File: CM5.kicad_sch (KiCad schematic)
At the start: 12 parts, among them J7 USB_B_Mini, J8 484060001, U6 Compute_Module_5_Functional

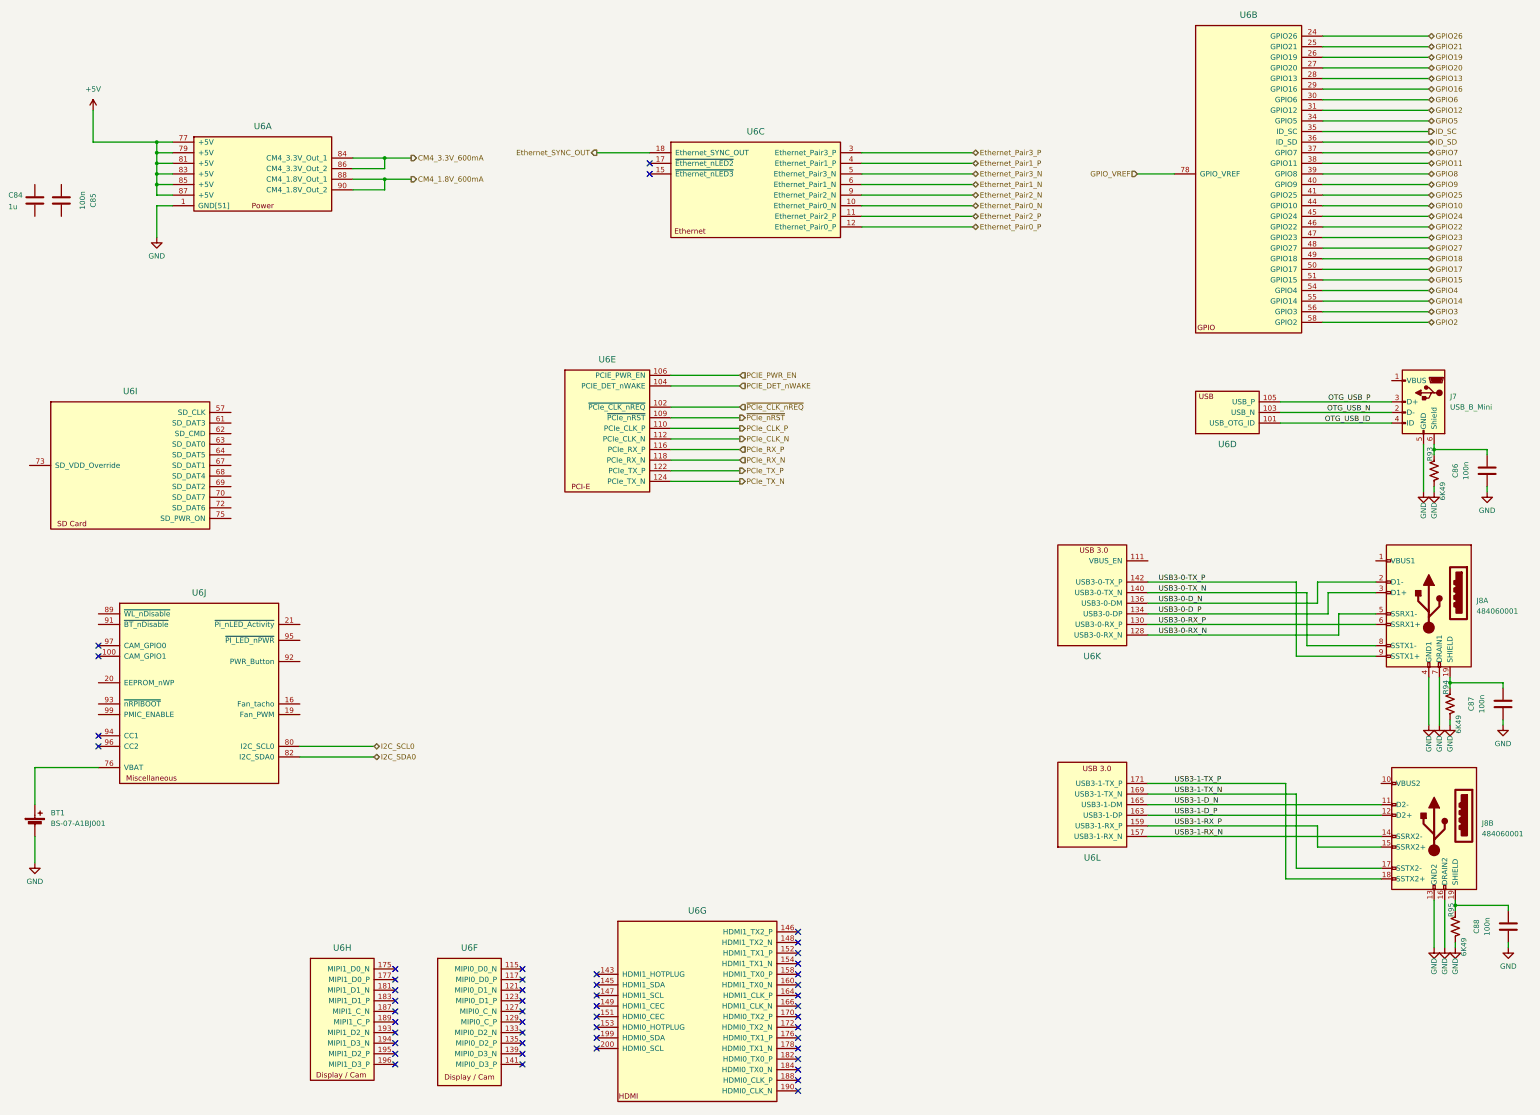
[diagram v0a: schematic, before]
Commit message: add impedance spec in the datasheet
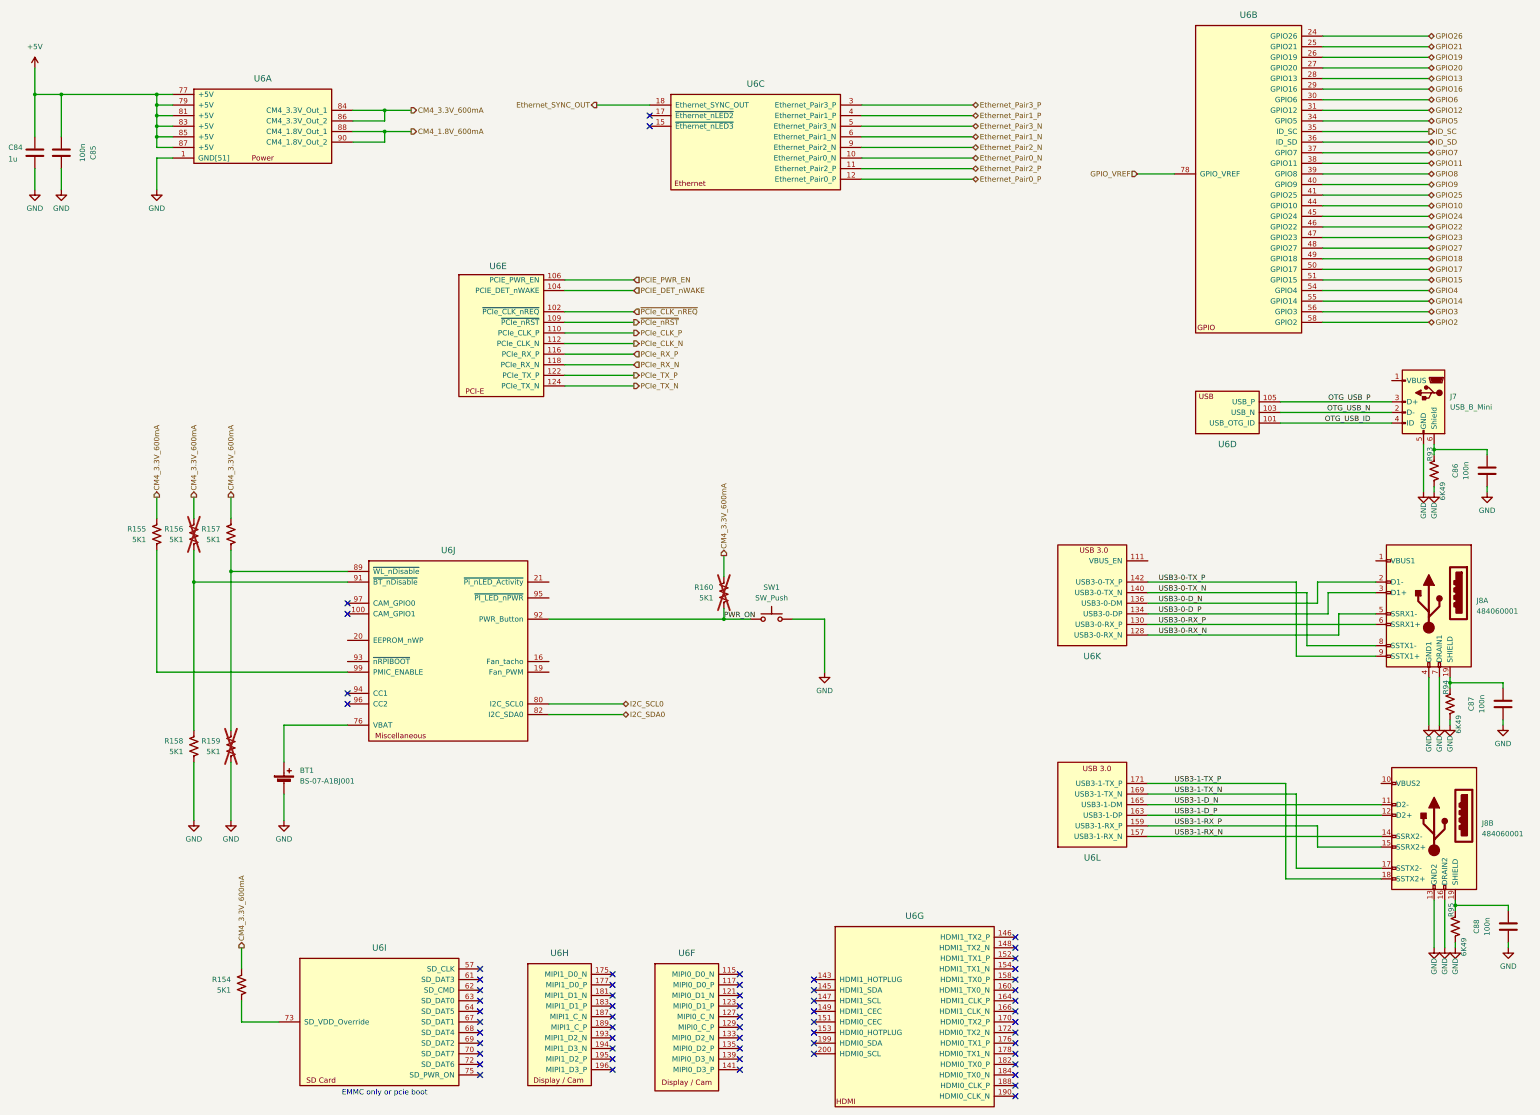
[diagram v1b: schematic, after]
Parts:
- added R154, R155, R156, R157, R158, R159, R160: 5K1, symbol Device:R_US
- added SW1: SW_Push, symbol Switch:SW_Push
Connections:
- net +5V: now also C84.1, C85.2
- net CM4_3.3V_600mA: now also R154.1, R155.1, R156.1, R157.1, R160.1
- net GND: now also C84.2, C85.1, R158.2, R159.2, SW1.2
- net at U6.73 (SD_VDD_Override): now also R154.2
- net at U6.89 (~{WL_nDisable}): now also R157.2, R159.1
- net at U6.91 (~{BT_nDisable}): now also R156.2, R158.1
- net PWR_ON: now reaches U6.92 (PWR_Button)
- net PWR_ON: now also R160.2, SW1.1
- net at U6.99 (PMIC_ENABLE): now also R155.2
- no-connect marks 50 -> 61
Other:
- note added: "EMMC only or pcie boot"
- moved on the sheet: BT1, C84, C85, U6A, U6C, U6E, U6F, U6G, U6H, U6I, U6J
